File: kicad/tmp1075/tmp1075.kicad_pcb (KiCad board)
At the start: 4 copper layers, 8.5 x 6 mm, 17 parts, among them J1 Conn_01x05, J2 Conn_01x05, U1 TMP1075DSG

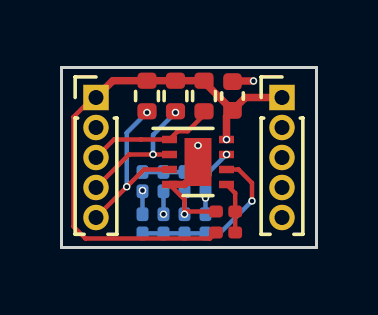
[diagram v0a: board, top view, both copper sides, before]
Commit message: take 2 on tmp1075 breakout
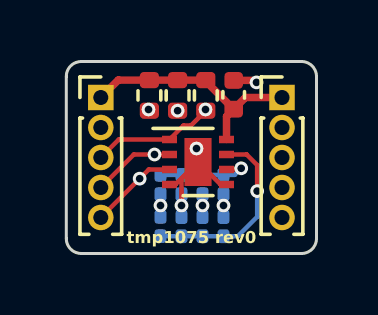
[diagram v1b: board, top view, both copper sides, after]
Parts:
- removed JP10, JP9: SolderJumper_2_Open, Resistor_SMD:R_0201_0603Metric
- moved JP1 3.09 mm to (153.9, 97.9), turned to 90 degrees
- moved JP5 3.00 mm to (153.9, 96.5), turned to -90 degrees
- moved JP4 2.11 mm to (151.8, 97.9), turned to 90 degrees
- moved JP8 1.99 mm to (151.8, 96.5), turned to -90 degrees
- moved JP2 1.98 mm to (153.2, 97.9), turned to 90 degrees
- moved JP6 1.85 mm to (153.2, 96.5), turned to -90 degrees
- moved JP3 1.50 mm to (152.5, 97.9), turned to 90 degrees
- moved JP7 1.31 mm to (152.5, 96.5), turned to -90 degrees
- moved J1 0.16 mm to (149.8, 93.6)
- moved R3 0.08 mm to (151.4, 93.5)
- moved R2 0.07 mm to (152.4, 93.5)
- moved R1 0.06 mm to (153.3, 93.5)
- moved C1 0.06 mm to (154.2, 93.5)
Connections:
- U1 pad 5: /A2 -> GND
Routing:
- net +3V3: track 20.8 -> 13.4 mm, vias 2 -> 1
- net /A0: track 3.05 -> 6.39 mm
- net /A1: track 5.73 -> 3.29 mm
- net /A2: track 1.72 -> 0.00 mm
- net /SDA: track 12.3 -> 11.1 mm, vias 1 -> 2
- net /ALERT: track 13.0 -> 12.0 mm
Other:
- board size 8.5 x 6 mm -> 8.3 x 6.4 mm
- board text added: "tmp1075 rev0"
- board text added: "⚧"
